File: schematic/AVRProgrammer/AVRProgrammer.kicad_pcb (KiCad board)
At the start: 2 copper layers, 40 parts, among them J1 ProMicro_L, J2 ProMicro_R, J3 ProgConn, Q1 BSS138, SW1 Reset, SW2 PowerSelect, U1 LM1117-3.3, U2 MC74VHC1GT125, U3 MC74VHC1GT125, U4 MC74VHC1GT125, U5 MC74VHC1GT125, U6 MC74VHC1GT125, U7 MC74VHC1GT125

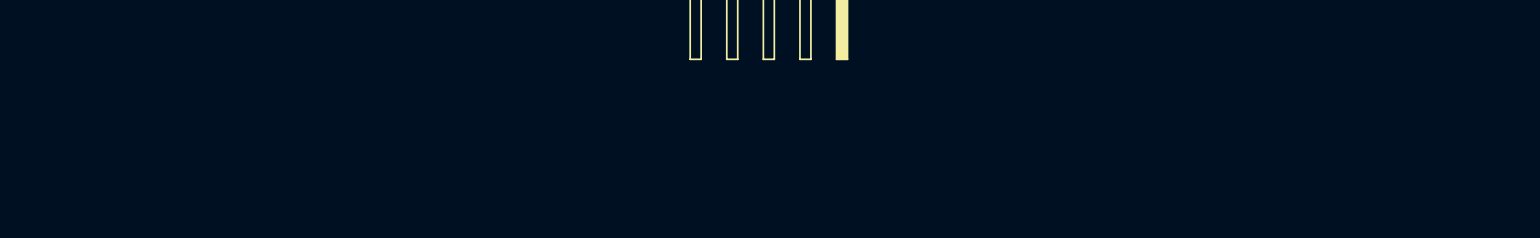
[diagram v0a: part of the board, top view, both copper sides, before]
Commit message: Add warning to PCB. Add .gitignore
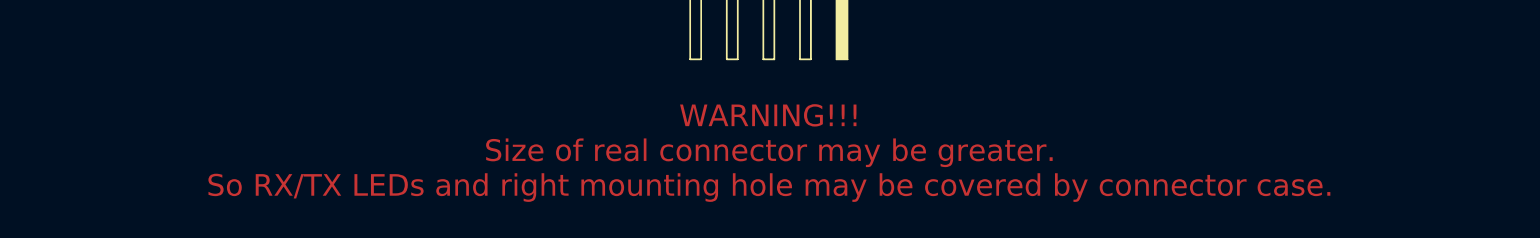
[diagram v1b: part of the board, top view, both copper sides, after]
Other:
- board text added: "WARNING!!! Size of real connector may be greater. So RX/TX LEDs and right mounting hole may be covered by connector case."
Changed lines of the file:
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@@
   (general
     (thickness 1.6)
-    (drawings 4)
+    (drawings 5)
     (tracks 307)
     (zones 0)
@@
     )
   )
+  (gr_text "WARNING!!!\nSize of real connector may be greater.\nSo RX/TX LEDs and right mounting hole may be covered by connector case." (at 137 139) (layer F.Cu)
+    (effects (font (size 1.5 1.5) (thickness 0.3)))
+  )
   (target plus (at 122 123) (size 5) (width 0.15) (layer Edge.Cuts))

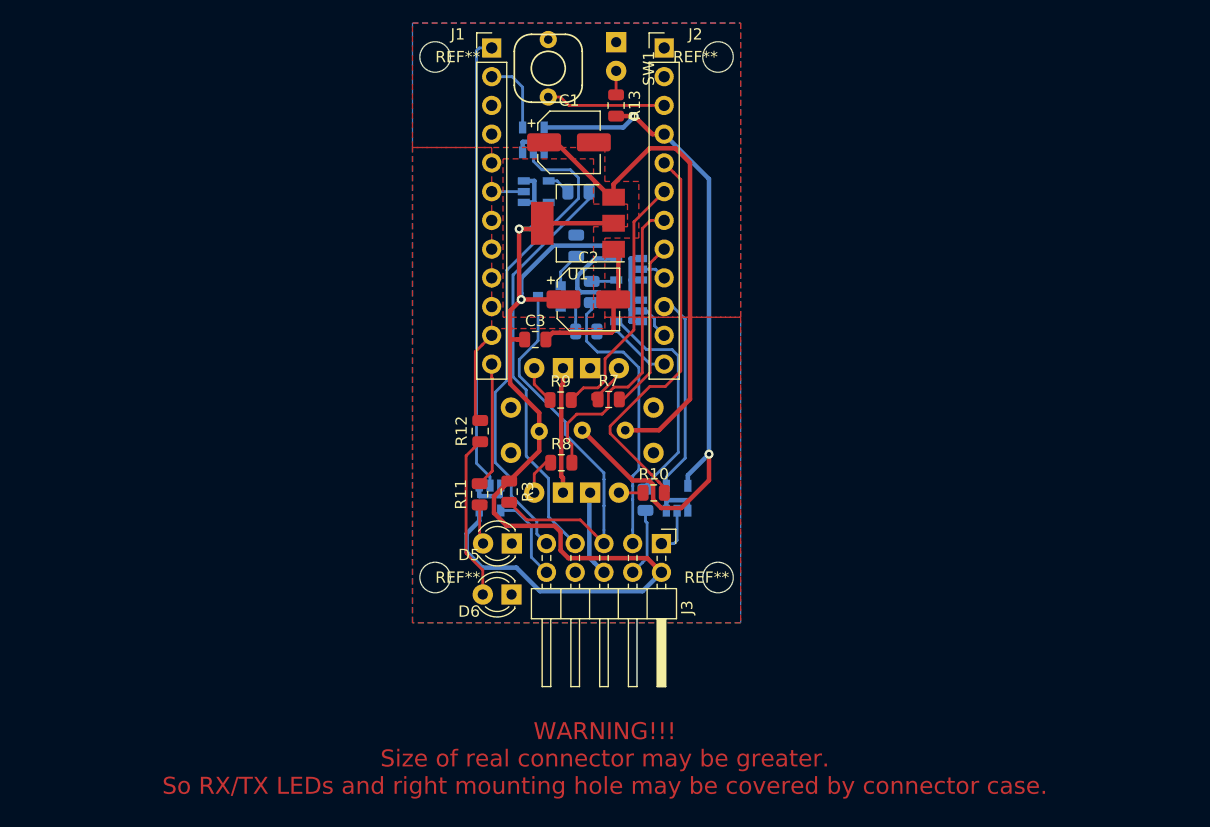
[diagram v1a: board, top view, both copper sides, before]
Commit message: 3dmodels for PCB components was added
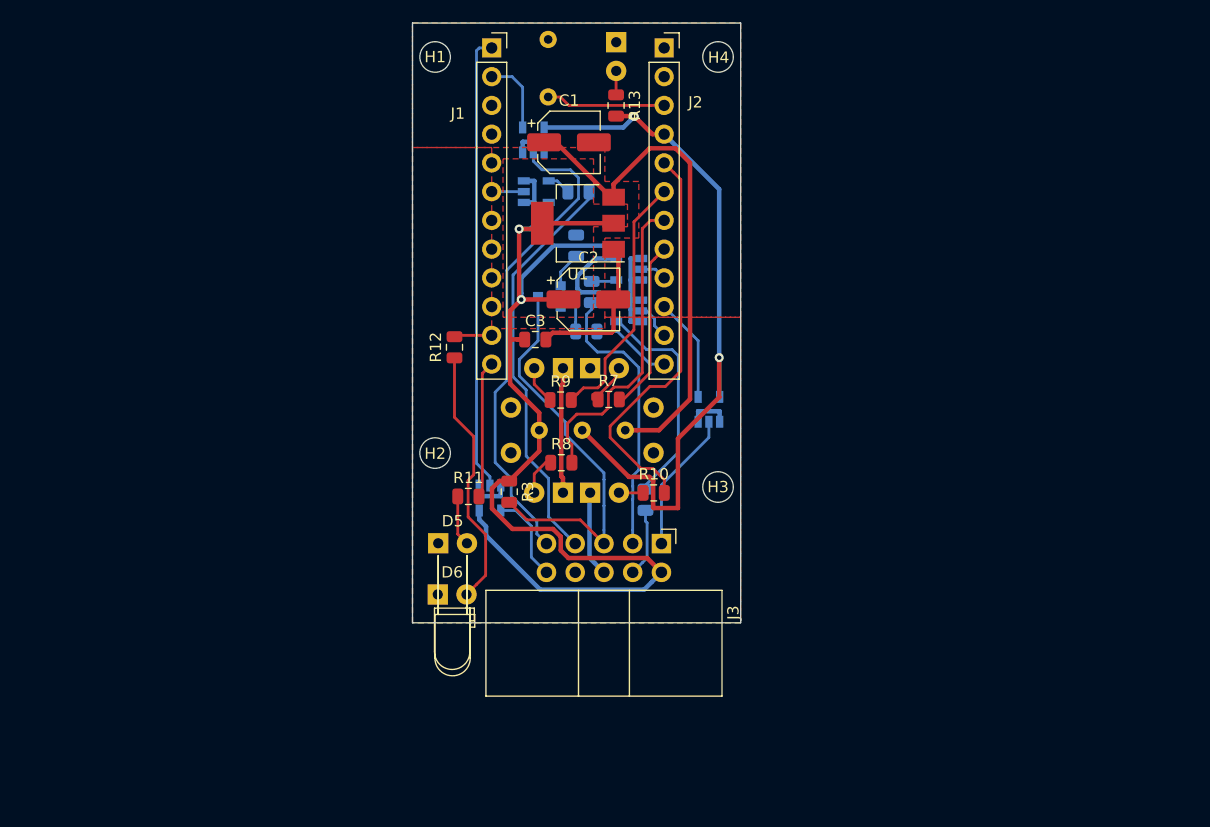
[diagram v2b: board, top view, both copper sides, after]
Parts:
- removed REF**: 3, MountingHole:MountingHole_2.7mm_M2.5
- removed REF**: 4, MountingHole:MountingHole_2.7mm_M2.5
- removed REF**: 2, MountingHole:MountingHole_2.7mm_M2.5
- removed REF**: 1, MountingHole:MountingHole_2.7mm_M2.5
- added H1: 1, MountingHole:MountingHole_2.7mm_M2.5, F.Cu at (122.0, 77.0)
- added H2: 1, MountingHole:MountingHole_2.7mm_M2.5, F.Cu at (122.0, 112.0)
- added H3: 1, MountingHole:MountingHole_2.7mm_M2.5, F.Cu at (147.0, 115.0)
- added H4: 1, MountingHole:MountingHole_2.7mm_M2.5, F.Cu at (147.0, 77.0)
- D5: footprint LED_THT:LED_D3.0mm -> LED_THT:LED_D3.0mm_Horizontal_O6.35mm_Z6.0mm
- D6: footprint LED_THT:LED_D3.0mm -> LED_THT:LED_D3.0mm_Horizontal_O1.27mm_Z2.0mm
- J1, J2: footprint Connector_PinHeader_2.54mm:PinHeader_1x12_P2.54mm_Vertical -> Connector_PinSocket_2.54mm:PinSocket_1x12_P2.54mm_Vertical
- J3: footprint Connector_PinHeader_2.54mm:PinHeader_2x05_P2.54mm_Horizontal -> Connector_IDC:IDC-Header_2x05_P2.54mm_Horizontal
- SW1: moved to B.Cu
- moved U3 8.35 mm to (146.2, 108.1)
- moved R12 7.75 mm to (123.7, 102.7)
- moved D6 6.52 mm to (122.2, 124.5), turned to 0 degrees
- moved D5 6.50 mm to (122.3, 120.0), turned to 0 degrees
- moved R11 1.01 mm to (124.9, 115.8), turned to 0 degrees
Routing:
- net Net-(D6-Pad2): track 14.6 -> 23.2 mm
- net MISO: track 17.7 -> 9.22 mm
- net MISO_P: track 4.12 -> 12.5 mm
- net LED_TX: track 8.30 -> 3.34 mm
- net VCC_P: track 108.3 -> 105.7 mm
- net LED_RX: track 11.0 -> 12.6 mm
- net VCC: track 64.9 -> 66.0 mm
- net LED_ACT: track 35.1 -> 35.8 mm
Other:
- board outline added: 29 x 53 mm
- board text removed: "WARNING!!! Size of real connector may be greater. So RX/TX LEDs and right mounting hole may be covered by connector case."
